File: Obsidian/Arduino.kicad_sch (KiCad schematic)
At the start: 17 parts

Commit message: update with available components on LCSC
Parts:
- R123, R129, R133, R137: LCSC (none) -> C25081
- R124, R130, R134, R138: LCSC (none) -> C1509615
- R125, R127, R131, R135: LCSC (none) -> C82297
- R126, R128, R132, R136: LCSC (none) -> C11702

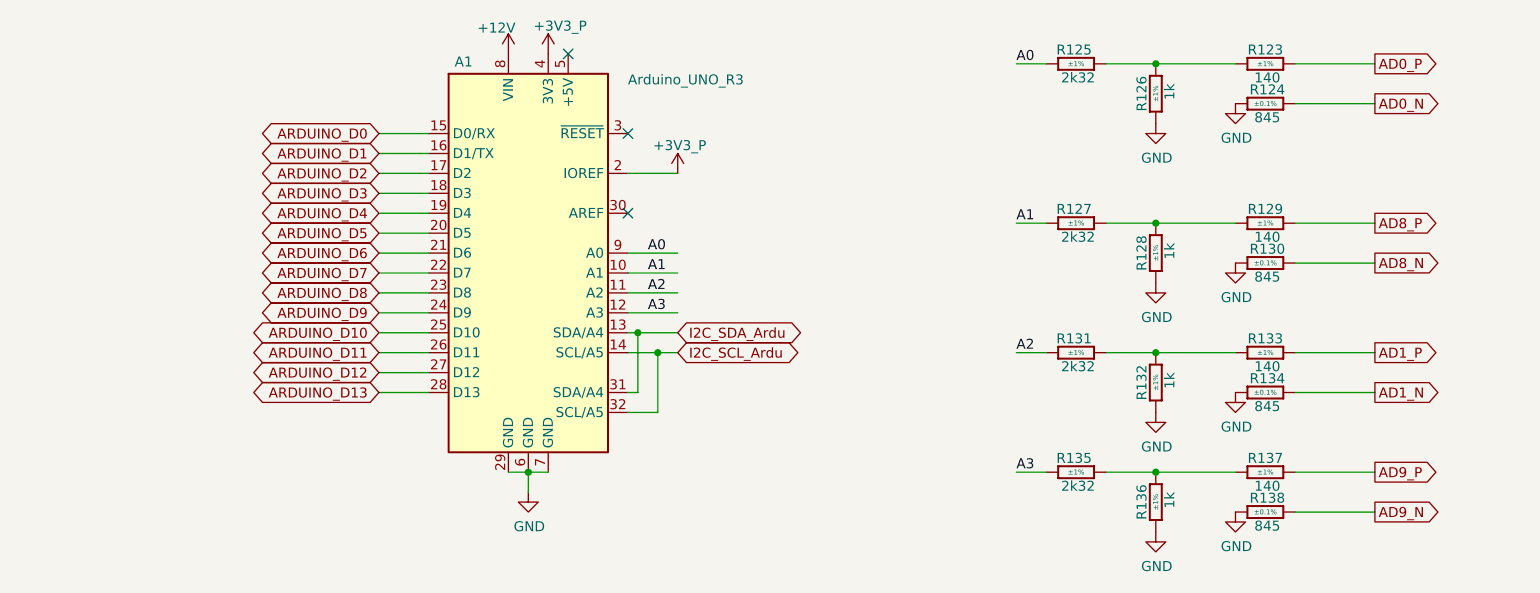
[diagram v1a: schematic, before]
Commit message: replacing global label with hierarchical label
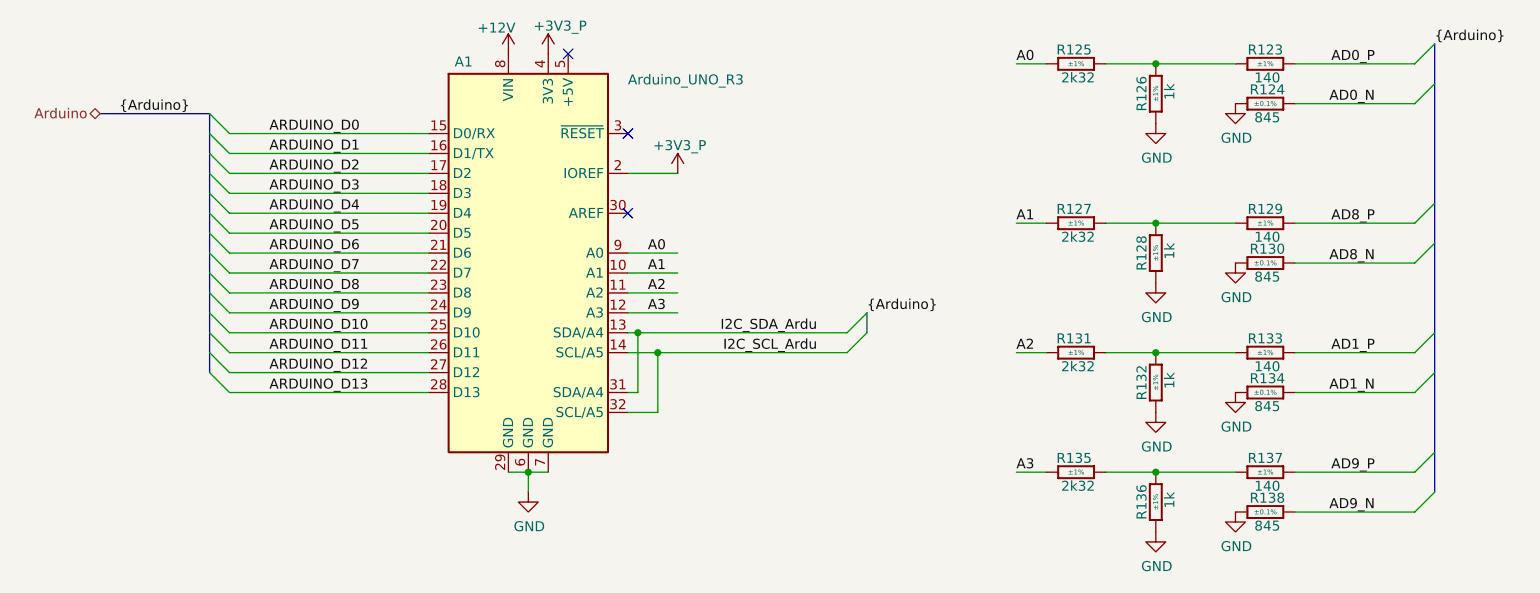
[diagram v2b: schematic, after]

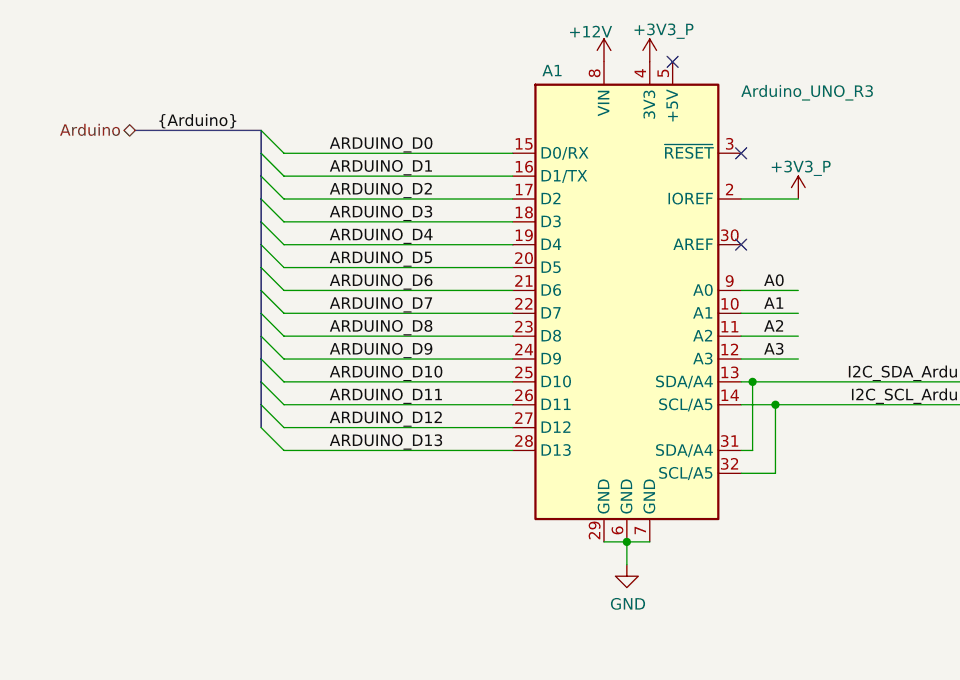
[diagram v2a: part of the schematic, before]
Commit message: Adding symbol library
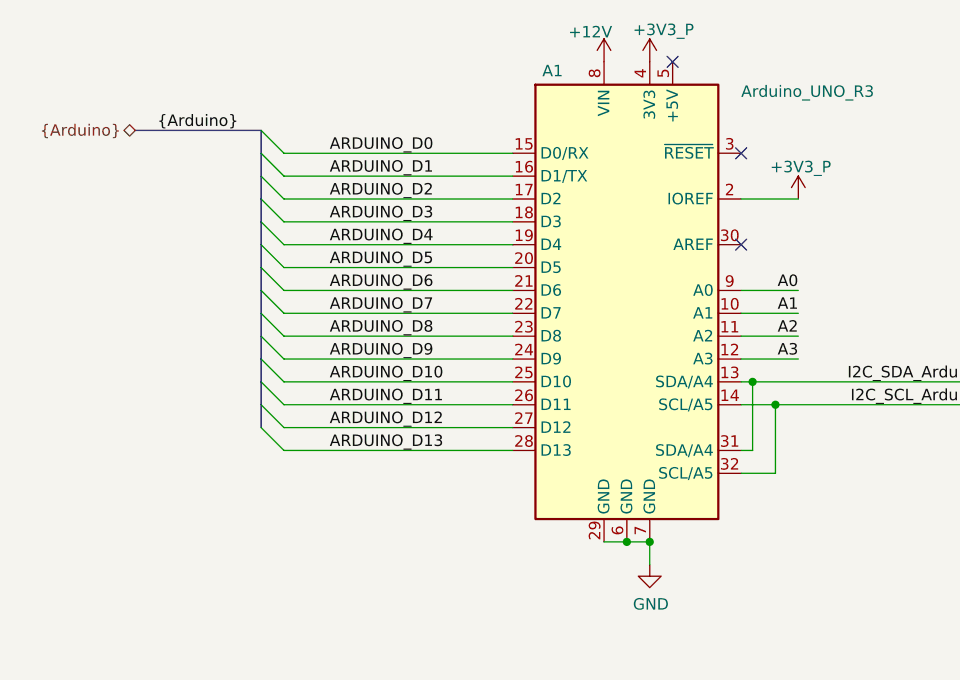
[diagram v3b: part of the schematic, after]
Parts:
- A1: symbol MCU_Module:Arduino_UNO_R3 -> Library_Symbol:Arduino_UNO_R3
- R123, R129, R133, R137: symbol Resistors SMD:R0402_140R_1%_0.0625W_100PPM -> Library_Symbol:R0402_140R_1%_0.0625W_100PPM
- R124, R130, R134, R138: symbol Resistors SMD:R0402_820R_0.1%_0.063W_25PPM -> Library_Symbol:R0402_820R_0.1%_0.063W_25PPM
- R125, R127, R131, R135: symbol Resistors SMD:R0402_2K_1%_0.0625W_100PPM -> Library_Symbol:R0402_2K_1%_0.0625W_100PPM
- R126, R128, R132, R136: symbol Resistors SMD:R0402_1K_1%_0.0625W_100PPM -> Library_Symbol:R0402_1K_1%_0.0625W_100PPM
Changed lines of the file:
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@@
 	)
 	(junction
+		(at 140.97 113.03)
+		(diameter 0)
+		(color 0 0 0 0)
+	)
+	(junction
 		(at 138.43 113.03)
 		(diameter 0)
@@
 	(wire
 		(pts
-			(xy 138.43 113.03) (xy 138.43 115.57)
+			(xy 140.97 113.03) (xy 140.97 115.57)
 		)
 		(stroke
@@
 	(wire
 		(pts
-			(xy 138.43 113.03) (xy 140.97 113.03)
-		)
-		(stroke
-			(width 0)
-			(type default)
-		)
-	)
-	(wire
-		(pts
 			(xy 212.09 60.96) (xy 218.44 60.96)
 		)
@@
 		)
 	)
+	(wire
+		(pts
+			(xy 140.97 113.03) (xy 138.43 113.03)
+		)
+		(stroke
+			(width 0)
+			(type default)
+		)
+	)
 	(bus
 		(pts
@@
 	)
 	(label "A1"
-		(at 153.67 87.63 0)
+		(at 157.48 87.63 180)
 		(effects
 			(font
 				(size 1.27 1.27)
 			)
-			(justify left bottom)
+			(justify right bottom)
 		)
 	)
@@
 	)
 	(label "A3"
-		(at 153.67 92.71 0)
+		(at 157.48 92.71 180)
 		(effects
 			(font
 				(size 1.27 1.27)
 			)
-			(justify left bottom)
+			(justify right bottom)
 		)
 	)
@@
 	)
 	(label "A0"
-		(at 153.67 85.09 0)
+		(at 157.48 85.09 180)
 		(effects
 			(font
 				(size 1.27 1.27)
 			)
-			(justify left bottom)
+			(justify right bottom)
 		)
 	)
@@
 	)
 	(label "A2"
-		(at 153.67 90.17 0)
+		(at 157.48 90.17 180)
 		(effects
 			(font
 				(size 1.27 1.27)
 			)
-			(justify left bottom)
+			(justify right bottom)
 		)
 	)
@@
 		)
 	)
-	(hierarchical_label "Arduino"
+	(hierarchical_label "{Arduino}"
 		(shape bidirectional)
 		(at 83.82 67.31 180)
@@
 	)
 	(symbol
-		(lib_id "Resistors SMD:R0402_820R_0.1%_0.063W_25PPM")
+		(lib_id "Library_Symbol:R0402_820R_0.1%_0.063W_25PPM")
 		(at 228.6 102.87 0)
 		(unit 1)
@@
 	)
 	(symbol
-		(lib_id "Resistors SMD:R0402_140R_1%_0.0625W_100PPM")
+		(lib_id "Library_Symbol:R0402_140R_1%_0.0625W_100PPM")
 		(at 228.6 113.03 0)
 		(unit 1)
@@
 	)
 	(symbol
-		(lib_id "Resistors SMD:R0402_2K_1%_0.0625W_100PPM")
+		(lib_id "Library_Symbol:R0402_2K_1%_0.0625W_100PPM")
 		(at 204.47 97.79 0)
 		(unit 1)
@@
 	)
 	(symbol
-		(lib_id "Resistors SMD:R0402_2K_1%_0.0625W_100PPM")
+		(lib_id "Library_Symbol:R0402_2K_1%_0.0625W_100PPM")
 		(at 204.47 60.96 0)
 		(unit 1)
@@
 	)
 	(symbol
-		(lib_id "power:GND")
+		(lib_id "Library_Symbol:GND")
 		(at 218.44 68.58 0)
 		(unit 1)
@@
 	)
 	(symbol
-		(lib_id "Resistors SMD:R0402_140R_1%_0.0625W_100PPM")
+		(lib_id "Library_Symbol:R0402_140R_1%_0.0625W_100PPM")
 		(at 228.6 60.96 0)
 		(unit 1)
@@
 	)
 	(symbol
-		(lib_id "Resistors SMD:R0402_2K_1%_0.0625W_100PPM")
+		(lib_id "Library_Symbol:R0402_2K_1%_0.0625W_100PPM")
 		(at 204.47 113.03 0)
 		(unit 1)
@@
 	)
 	(symbol
-		(lib_id "Resistors SMD:R0402_1K_1%_0.0625W_100PPM")
+		(lib_id "Library_Symbol:R0402_1K_1%_0.0625W_100PPM")
 		(at 218.44 113.03 270)
 		(unit 1)
@@
 	)
 	(symbol
-		(lib_id "MCU_Module:Arduino_UNO_R3")
+		(lib_id "Library_Symbol:Arduino_UNO_R3")
 		(at 138.43 85.09 0)
 		(unit 1)
@@
 	)
 	(symbol
-		(lib_id "power:+12V")
+		(lib_id "Library_Symbol:+12V")
 		(at 135.89 59.69 0)
 		(unit 1)
@@
 	)
 	(symbol
-		(lib_id "power:+1V0")
+		(lib_id "Library_Symbol:+1V0")
 		(at 157.48 74.93 0)
 		(unit 1)
@@
 	)
 	(symbol
-		(lib_id "power:GND")
+		(lib_id "Library_Symbol:GND")
 		(at 228.6 118.11 0)
 		(unit 1)
@@
 	)
 	(symbol
-		(lib_id "power:GND")
+		(lib_id "Library_Symbol:GND")
 		(at 218.44 88.9 0)
 		(unit 1)
@@
 	)
 	(symbol
-		(lib_id "Resistors SMD:R0402_1K_1%_0.0625W_100PPM")
+		(lib_id "Library_Symbol:R0402_1K_1%_0.0625W_100PPM")
 		(at 218.44 81.28 270)
 		(unit 1)
@@
 	)
 	(symbol
-		(lib_id "power:GND")
+		(lib_id "Library_Symbol:GND")
 		(at 218.44 120.65 0)
 		(unit 1)
@@
 	)
 	(symbol
-		(lib_id "Resistors SMD:R0402_140R_1%_0.0625W_100PPM")
+		(lib_id "Library_Symbol:R0402_140R_1%_0.0625W_100PPM")
 		(at 228.6 97.79 0)
 		(unit 1)
@@
 	)
 	(symbol
-		(lib_id "Resistors SMD:R0402_820R_0.1%_0.063W_25PPM")
+		(lib_id "Library_Symbol:R0402_820R_0.1%_0.063W_25PPM")
 		(at 228.6 118.11 0)
 		(unit 1)
@@
 	)
 	(symbol
-		(lib_id "power:GND")
+		(lib_id "Library_Symbol:GND")
 		(at 228.6 66.04 0)
 		(unit 1)
@@
 	)
 	(symbol
-		(lib_id "Resistors SMD:R0402_820R_0.1%_0.063W_25PPM")
+		(lib_id "Library_Symbol:R0402_820R_0.1%_0.063W_25PPM")
 		(at 228.6 66.04 0)
 		(unit 1)
@@
 	)
 	(symbol
-		(lib_id "power:GND")
+		(lib_id "Library_Symbol:GND")
 		(at 228.6 102.87 0)
 		(unit 1)
@@
 	)
 	(symbol
-		(lib_id "Resistors SMD:R0402_1K_1%_0.0625W_100PPM")
+		(lib_id "Library_Symbol:R0402_1K_1%_0.0625W_100PPM")
 		(at 218.44 60.96 270)
 		(unit 1)
@@
 	)
 	(symbol
-		(lib_id "power:GND")
+		(lib_id "Library_Symbol:GND")
 		(at 228.6 86.36 0)
 		(unit 1)
@@
 	)
 	(symbol
-		(lib_id "Resistors SMD:R0402_2K_1%_0.0625W_100PPM")
+		(lib_id "Library_Symbol:R0402_2K_1%_0.0625W_100PPM")
 		(at 204.47 81.28 0)
 		(unit 1)
@@
 	)
 	(symbol
-		(lib_id "power:GND")
+		(lib_id "Library_Symbol:GND")
 		(at 218.44 105.41 0)
 		(unit 1)
@@
 	)
 	(symbol
-		(lib_id "Resistors SMD:R0402_140R_1%_0.0625W_100PPM")
+		(lib_id "Library_Symbol:R0402_140R_1%_0.0625W_100PPM")
 		(at 228.6 81.28 0)
 		(unit 1)
@@
 	)
 	(symbol
-		(lib_id "power:+1V0")
+		(lib_id "Library_Symbol:+1V0")
 		(at 140.97 59.69 0)
 		(unit 1)
@@
 	)
 	(symbol
-		(lib_id "Resistors SMD:R0402_820R_0.1%_0.063W_25PPM")
+		(lib_id "Library_Symbol:R0402_820R_0.1%_0.063W_25PPM")
 		(at 228.6 86.36 0)
 		(unit 1)
@@
 	)
 	(symbol
-		(lib_id "Resistors SMD:R0402_1K_1%_0.0625W_100PPM")
+		(lib_id "Library_Symbol:R0402_1K_1%_0.0625W_100PPM")
 		(at 218.44 97.79 270)
 		(unit 1)
@@
 	)
 	(symbol
-		(lib_id "power:GND")
-		(at 138.43 115.57 0)
+		(lib_id "Library_Symbol:GND")
+		(at 140.97 115.57 0)
 		(unit 1)
 		(exclude_from_sim no)
@@
 		(dnp no)
 		(property "Reference" "#PWR0284"
-			(at 138.43 121.92 0)
+			(at 140.97 121.92 0)
 			(effects
 				(font
@@
 		)
 		(property "Value" "GND"
-			(at 138.557 119.9642 0)
+			(at 141.097 119.9642 0)
 			(effects
 				(font
@@
 		)
 		(property "Footprint" ""
-			(at 138.43 115.57 0)
+			(at 140.97 115.57 0)
 			(effects
 				(font
@@
 		)
 		(property "Datasheet" ""
-			(at 138.43 115.57 0)
+			(at 140.97 115.57 0)
 			(effects
 				(font
@@
 		)
 		(property "Description" ""
-			(at 138.43 115.57 0)
+			(at 140.97 115.57 0)
 			(effects
 				(font

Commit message: Correct Schematic errors
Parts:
- A1: footprint Module:Arduino_UNO_R3 -> Footprint:Arduino_UNO_R3
- R123, R124, R125, R126, R127, R128, R129, R130, R131, R132, R133, R134, R135, R136, R137, R138: footprint Resistors SMD:RESC1005X40N -> Footprint:RESC1005X40N
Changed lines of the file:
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@@
 			)
 		)
-		(property "Footprint" "Resistors SMD:RESC1005X40N"
+		(property "Footprint" "Footprint:RESC1005X40N"
 			(at 228.6 109.728 0)
 			(effects
@@
 			)
 		)
-		(property "Footprint" "Resistors SMD:RESC1005X40N"
+		(property "Footprint" "Footprint:RESC1005X40N"
 			(at 228.6 119.888 0)
 			(effects
@@
 			)
 		)
-		(property "Footprint" "Resistors SMD:RESC1005X40N"
+		(property "Footprint" "Footprint:RESC1005X40N"
 			(at 204.47 104.648 0)
 			(effects
@@
 			)
 		)
-		(property "Footprint" "Resistors SMD:RESC1005X40N"
+		(property "Footprint" "Footprint:RESC1005X40N"
 			(at 204.47 67.818 0)
 			(effects
@@
 			)
 		)
-		(property "Footprint" "Resistors SMD:RESC1005X40N"
+		(property "Footprint" "Footprint:RESC1005X40N"
 			(at 228.6 67.818 0)
 			(effects
@@
 			)
 		)
-		(property "Footprint" "Resistors SMD:RESC1005X40N"
+		(property "Footprint" "Footprint:RESC1005X40N"
 			(at 204.47 119.888 0)
 			(effects
@@
 			)
 		)
-		(property "Footprint" "Resistors SMD:RESC1005X40N"
+		(property "Footprint" "Footprint:RESC1005X40N"
 			(at 211.582 113.03 0)
 			(effects
@@
 			)
 		)
-		(property "Footprint" "Module:Arduino_UNO_R3"
+		(property "Footprint" "Footprint:Arduino_UNO_R3"
 			(at 138.43 85.09 0)
 			(effects
@@
 			)
 		)
-		(property "Footprint" "Resistors SMD:RESC1005X40N"
+		(property "Footprint" "Footprint:RESC1005X40N"
 			(at 211.582 81.28 0)
 			(effects
@@
 			)
 		)
-		(property "Footprint" "Resistors SMD:RESC1005X40N"
+		(property "Footprint" "Footprint:RESC1005X40N"
 			(at 228.6 104.648 0)
 			(effects
@@
 			)
 		)
-		(property "Footprint" "Resistors SMD:RESC1005X40N"
+		(property "Footprint" "Footprint:RESC1005X40N"
 			(at 228.6 124.968 0)
 			(effects
@@
 			)
 		)
-		(property "Footprint" "Resistors SMD:RESC1005X40N"
+		(property "Footprint" "Footprint:RESC1005X40N"
 			(at 228.6 72.898 0)
 			(effects
@@
 			)
 		)
-		(property "Footprint" "Resistors SMD:RESC1005X40N"
+		(property "Footprint" "Footprint:RESC1005X40N"
 			(at 211.582 60.96 0)
 			(effects
@@
 			)
 		)
-		(property "Footprint" "Resistors SMD:RESC1005X40N"
+		(property "Footprint" "Footprint:RESC1005X40N"
 			(at 204.47 88.138 0)
 			(effects
@@
 			)
 		)
-		(property "Footprint" "Resistors SMD:RESC1005X40N"
+		(property "Footprint" "Footprint:RESC1005X40N"
 			(at 228.6 88.138 0)
 			(effects
@@
 			)
 		)
-		(property "Footprint" "Resistors SMD:RESC1005X40N"
+		(property "Footprint" "Footprint:RESC1005X40N"
 			(at 228.6 93.218 0)
 			(effects
@@
 			)
 		)
-		(property "Footprint" "Resistors SMD:RESC1005X40N"
+		(property "Footprint" "Footprint:RESC1005X40N"
 			(at 211.582 97.79 0)
 			(effects

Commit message: adding 3D files, 3D model of twist, and correct DRC
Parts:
- A1: Component Class (none) -> STACKED_SHIELD
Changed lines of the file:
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@@
+			)
+		)
+		(property "Component Class" "STACKED_SHIELD"
+			(at 138.43 85.09 0)
+			(effects
+				(font
+					(size 1.27 1.27)
+				)
+				(hide yes)
 			)
 		)

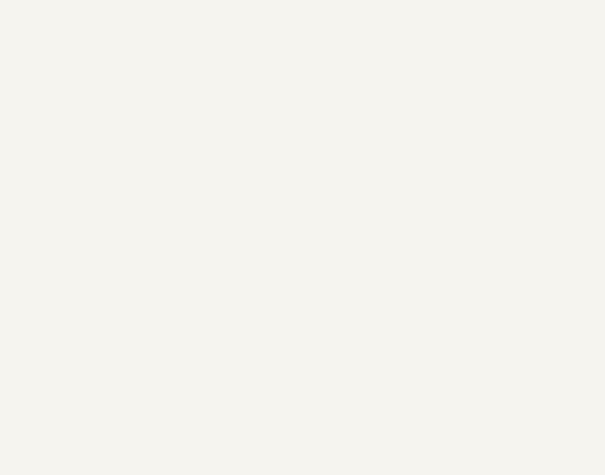
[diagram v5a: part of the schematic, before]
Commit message: adding pogo pins in the 3D model
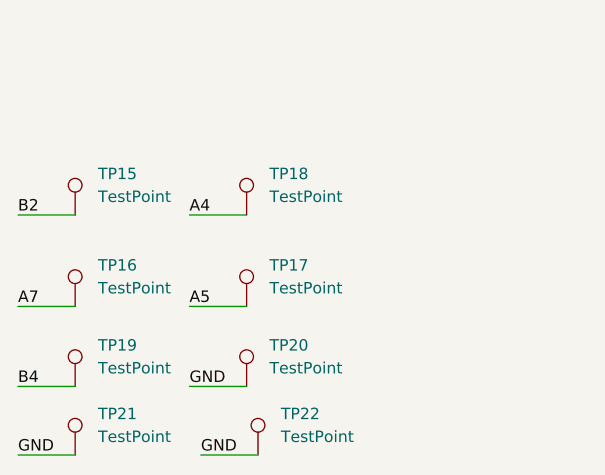
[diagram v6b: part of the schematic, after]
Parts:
- added TP15, TP16, TP17, TP18, TP19, TP20, TP21, TP22: TestPoint, TestPoint:TestPoint_Pad_D2.0mm, symbol Connector:TestPoint
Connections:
- net GND: now also TP20.1, TP21.1, TP22.1
- new net A4: TP18.1
- new net A5: TP17.1
- new net A7: TP16.1
- new net B2: TP15.1
- new net B4: TP19.1
